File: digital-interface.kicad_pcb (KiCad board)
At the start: 2 copper layers, 33 parts, among them U701 Si8641BD-B-IS2, U702 R05C05TE05S

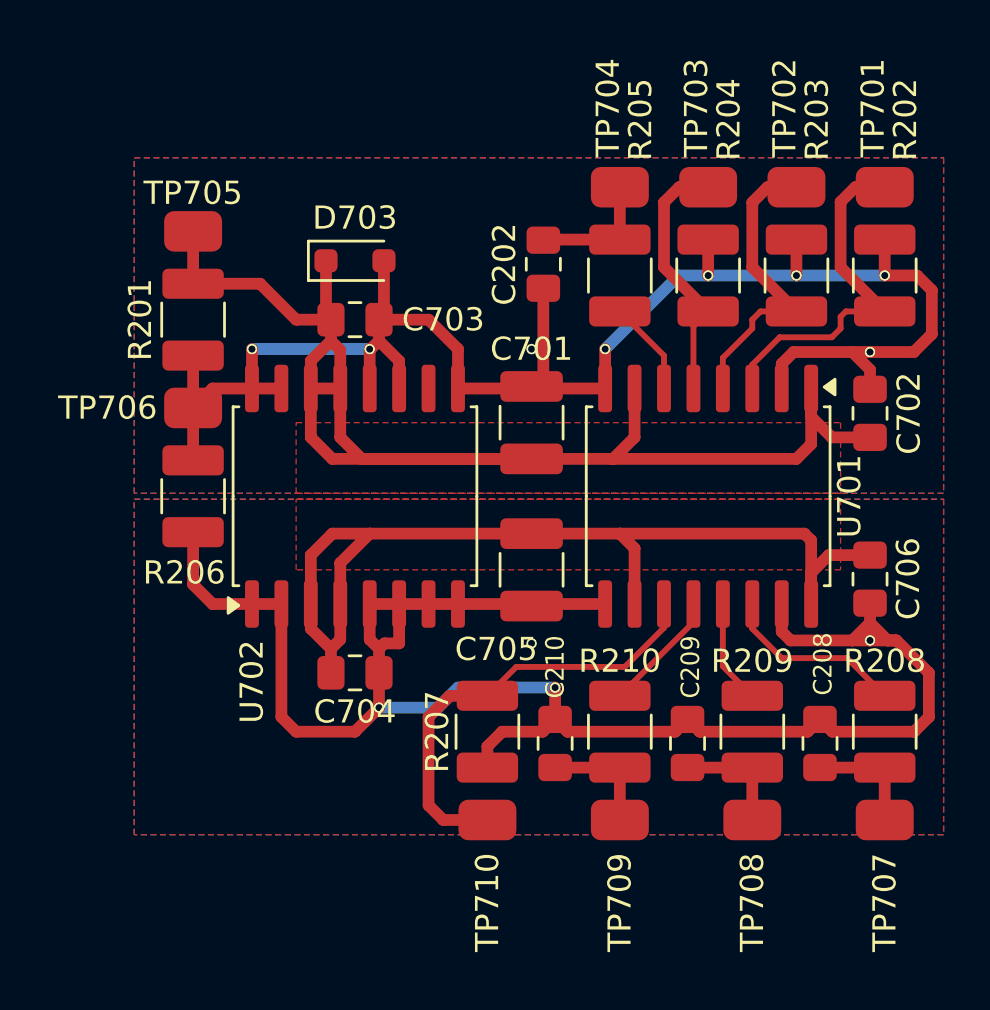
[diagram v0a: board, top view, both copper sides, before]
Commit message: separate digital-interface and iso-dcdc
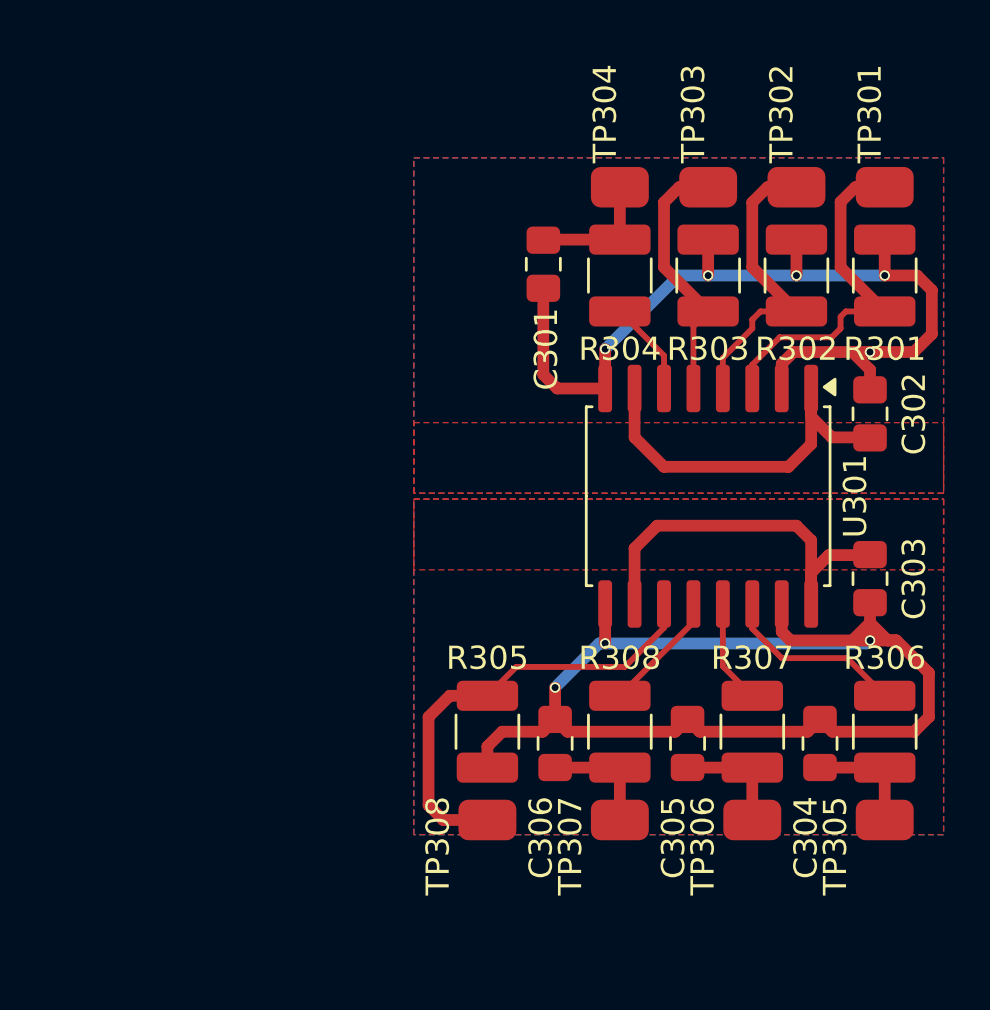
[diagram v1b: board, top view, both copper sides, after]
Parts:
- removed C701, C705: 10u, enclosure:C_1210_3225Metric_Pad1.33x2.70mm_HandSolder
- removed C702, C706: 100n, enclosure:C_0805_2012Metric_Pad1.18x1.45mm_HandSolder
- removed D703: PDZ5.6B115, enclosure:D_SOD-323_HandSoldering
- removed R201: 330, enclosure:R_1210_3225Metric_Pad1.30x2.65mm_HandSolder
- removed R206: 1M, enclosure:R_1210_3225Metric_Pad1.30x2.65mm_HandSolder
- removed TP705, TP706: ~, enclosure:TP_0805_2012Metric
- removed U702: R05C05TE05S, enclosure:SOIC-16W_7.5x10.3mm_P1.27mm
- C301: renamed from C202; footprint enclosure:C_0805_2012Metric_Pad1.18x1.45mm_HandSolder -> meas:C_0805_2012Metric_Pad1.18x1.45mm_HandSolder
- C302: renamed from C703; footprint enclosure:C_0805_2012Metric_Pad1.18x1.45mm_HandSolder -> meas:C_0805_2012Metric_Pad1.18x1.45mm_HandSolder
- C303: renamed from C704; footprint enclosure:C_0805_2012Metric_Pad1.18x1.45mm_HandSolder -> meas:C_0805_2012Metric_Pad1.18x1.45mm_HandSolder
- C304: renamed from C208; footprint enclosure:C_0805_2012Metric_Pad1.18x1.45mm_HandSolder -> meas:C_0805_2012Metric_Pad1.18x1.45mm_HandSolder
- C305: renamed from C209; footprint enclosure:C_0805_2012Metric_Pad1.18x1.45mm_HandSolder -> meas:C_0805_2012Metric_Pad1.18x1.45mm_HandSolder
- C306: renamed from C210; footprint enclosure:C_0805_2012Metric_Pad1.18x1.45mm_HandSolder -> meas:C_0805_2012Metric_Pad1.18x1.45mm_HandSolder
- R301: renamed from R202; footprint enclosure:R_1210_3225Metric_Pad1.30x2.65mm_HandSolder -> meas:R_1210_3225Metric_Pad1.30x2.65mm_HandSolder
- R302: renamed from R203; footprint enclosure:R_1210_3225Metric_Pad1.30x2.65mm_HandSolder -> meas:R_1210_3225Metric_Pad1.30x2.65mm_HandSolder
- R303: renamed from R204; footprint enclosure:R_1210_3225Metric_Pad1.30x2.65mm_HandSolder -> meas:R_1210_3225Metric_Pad1.30x2.65mm_HandSolder
- R304: renamed from R205; footprint enclosure:R_1210_3225Metric_Pad1.30x2.65mm_HandSolder -> meas:R_1210_3225Metric_Pad1.30x2.65mm_HandSolder
- R305: renamed from R207; footprint enclosure:R_1210_3225Metric_Pad1.30x2.65mm_HandSolder -> meas:R_1210_3225Metric_Pad1.30x2.65mm_HandSolder
- R306: renamed from R208; footprint enclosure:R_1210_3225Metric_Pad1.30x2.65mm_HandSolder -> meas:R_1210_3225Metric_Pad1.30x2.65mm_HandSolder
- R307: renamed from R209; footprint enclosure:R_1210_3225Metric_Pad1.30x2.65mm_HandSolder -> meas:R_1210_3225Metric_Pad1.30x2.65mm_HandSolder
- R308: renamed from R210; footprint enclosure:R_1210_3225Metric_Pad1.30x2.65mm_HandSolder -> meas:R_1210_3225Metric_Pad1.30x2.65mm_HandSolder
- TP301: renamed from TP701; footprint enclosure:TP_0805_2012Metric -> meas:TP_0805_2012Metric
- TP302: renamed from TP702; footprint enclosure:TP_0805_2012Metric -> meas:TP_0805_2012Metric
- TP303: renamed from TP703; footprint enclosure:TP_0805_2012Metric -> meas:TP_0805_2012Metric
- TP304: renamed from TP704; footprint enclosure:TP_0805_2012Metric -> meas:TP_0805_2012Metric
- TP305: renamed from TP707; footprint enclosure:TP_0805_2012Metric -> meas:TP_0805_2012Metric
- TP306: renamed from TP708; footprint enclosure:TP_0805_2012Metric -> meas:TP_0805_2012Metric
- TP307: renamed from TP709; footprint enclosure:TP_0805_2012Metric -> meas:TP_0805_2012Metric
- TP308: renamed from TP710; footprint enclosure:TP_0805_2012Metric -> meas:TP_0805_2012Metric
- U301: renamed from U701; footprint enclosure:SOIC-16W_7.5x10.3mm_P1.27mm -> meas:SOIC-16W_7.5x10.3mm_P1.27mm
- moved C302 22.6 mm to (90.8, 59.9), turned to -90 degrees
- moved C303 22.6 mm to (90.8, 67.1), turned to 90 degrees
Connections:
- net +5VA_digital-interface renamed /+5VA_SLAVE
- net +5VI renamed /+5VA_MASTER
- net /SCKL renamed /SCKL_SLAVE
- net /SCKL_ISO renamed /SCKL_MASTER
- net /SDI renamed /SDI_SLAVE
- net /SDI_ISO renamed /SDI_MASTER
- net /SDO renamed /SDO_SLAVE
- net /SDO_ISO renamed /SDO_MASTER
- net /~{CS_ISO} renamed /~{CS_MASTER}
- net /~{CS} renamed /~{CS_SLAVE}
- net GND renamed /GND_SLAVE
- net GNDI renamed /GND_MASTER
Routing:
- net /+5VA_MASTER: track 63.5 -> 17.2 mm
- net /GND_MASTER: track 73.4 -> 39.9 mm, vias 8 -> 5
- net /+5VA_SLAVE: track 43.4 -> 17.6 mm
- net /GND_SLAVE: track 79.2 -> 53.6 mm, vias 4 -> 3

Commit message: edit silkscreen
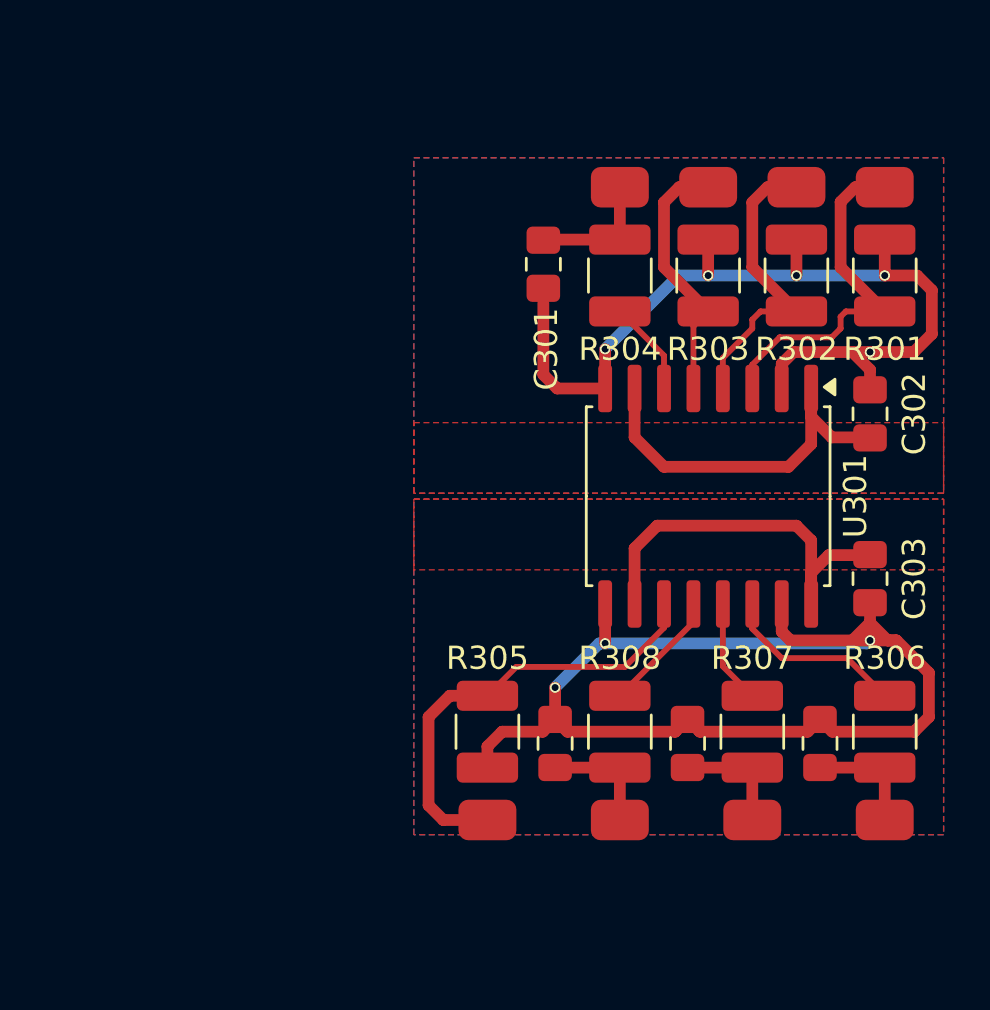
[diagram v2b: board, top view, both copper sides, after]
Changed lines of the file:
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@@
 			(at 0.635 3.175 90)
 			(layer "F.SilkS")
+			(hide yes)
 			(effects
 				(font
@@
 			(at 0.635 3.175 90)
 			(layer "F.SilkS")
+			(hide yes)
 			(effects
 				(font
@@
 			(at 4.064 0.6096 -90)
 			(layer "F.SilkS")
+			(hide yes)
 			(effects
 				(font
@@
 			(at -2.1336 1.1176 -90)
 			(layer "F.SilkS")
+			(hide yes)
 			(effects
 				(font
@@
 			(at 0 1.65 180)
 			(layer "F.Fab")
+			(hide yes)
 			(effects
 				(font
@@
 			(at -2.1336 1.1176 -90)
 			(layer "F.SilkS")
+			(hide yes)
 			(effects
 				(font
@@
 			(at 0 1.65 180)
 			(layer "F.Fab")
+			(hide yes)
 			(effects
 				(font
@@
 			(at 0.635 3.175 90)
 			(layer "F.SilkS")
+			(hide yes)
 			(effects
 				(font
@@
 			(at -2.1336 1.1176 -90)
 			(layer "F.SilkS")
+			(hide yes)
 			(effects
 				(font
@@
 			(at 0 1.65 180)
 			(layer "F.Fab")
+			(hide yes)
 			(effects
 				(font
@@
 			(at 0.635 3.175 90)
 			(layer "F.SilkS")
+			(hide yes)
 			(effects
 				(font
@@
 			(at 4.064 0.6096 -90)
 			(layer "F.SilkS")
+			(hide yes)
 			(effects
 				(font
@@
 			(at 4.064 0.6096 -90)
 			(layer "F.SilkS")
+			(hide yes)
 			(effects
 				(font
@@
 			(at -2.1336 1.1176 -90)
 			(layer "F.SilkS")
+			(hide yes)
 			(effects
 				(font
@@
 			(at 0 1.65 180)
 			(layer "F.Fab")
+			(hide yes)
 			(effects
 				(font
